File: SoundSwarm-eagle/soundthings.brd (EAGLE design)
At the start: 100 x 40 mm, 34 parts, among them Q1 IRLIB9343PbF, Q2 IRLB8721PBF, Q4 IRLB8721PBF

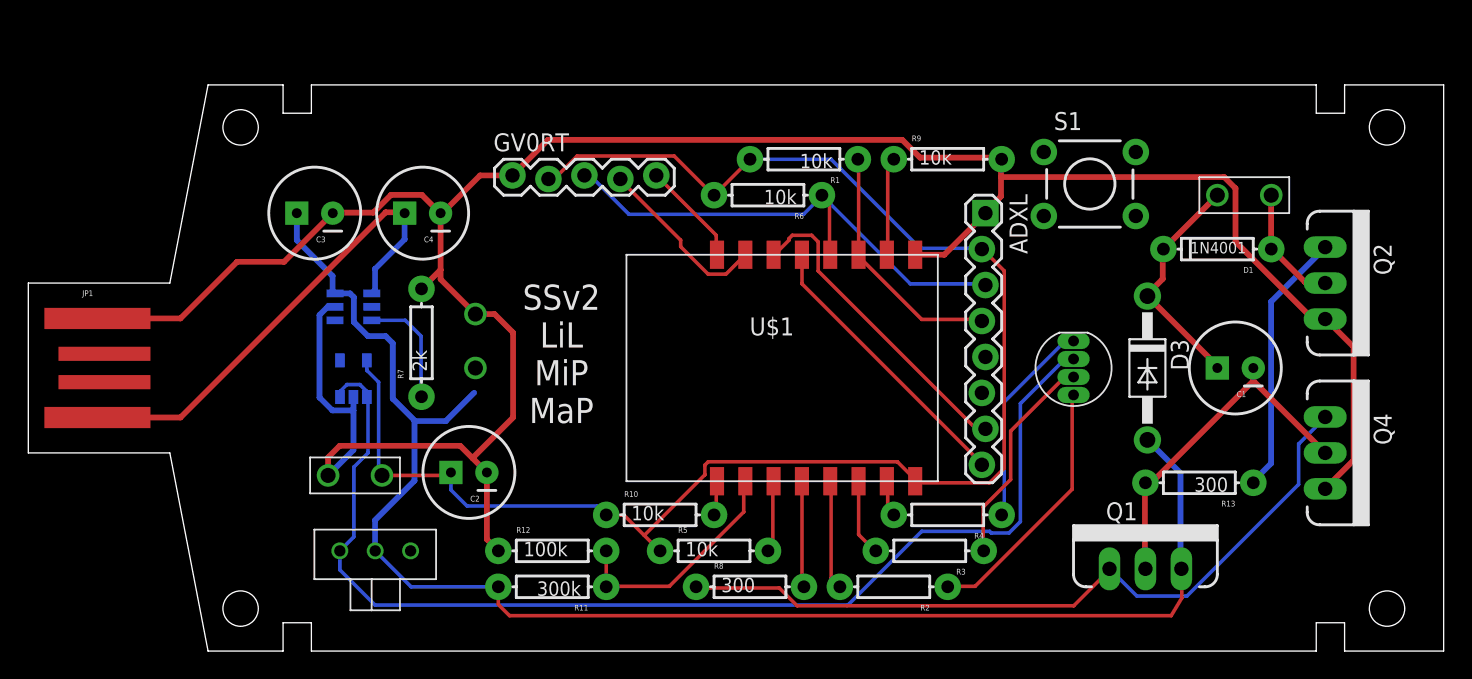
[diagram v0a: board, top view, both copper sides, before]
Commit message: removed names and added values
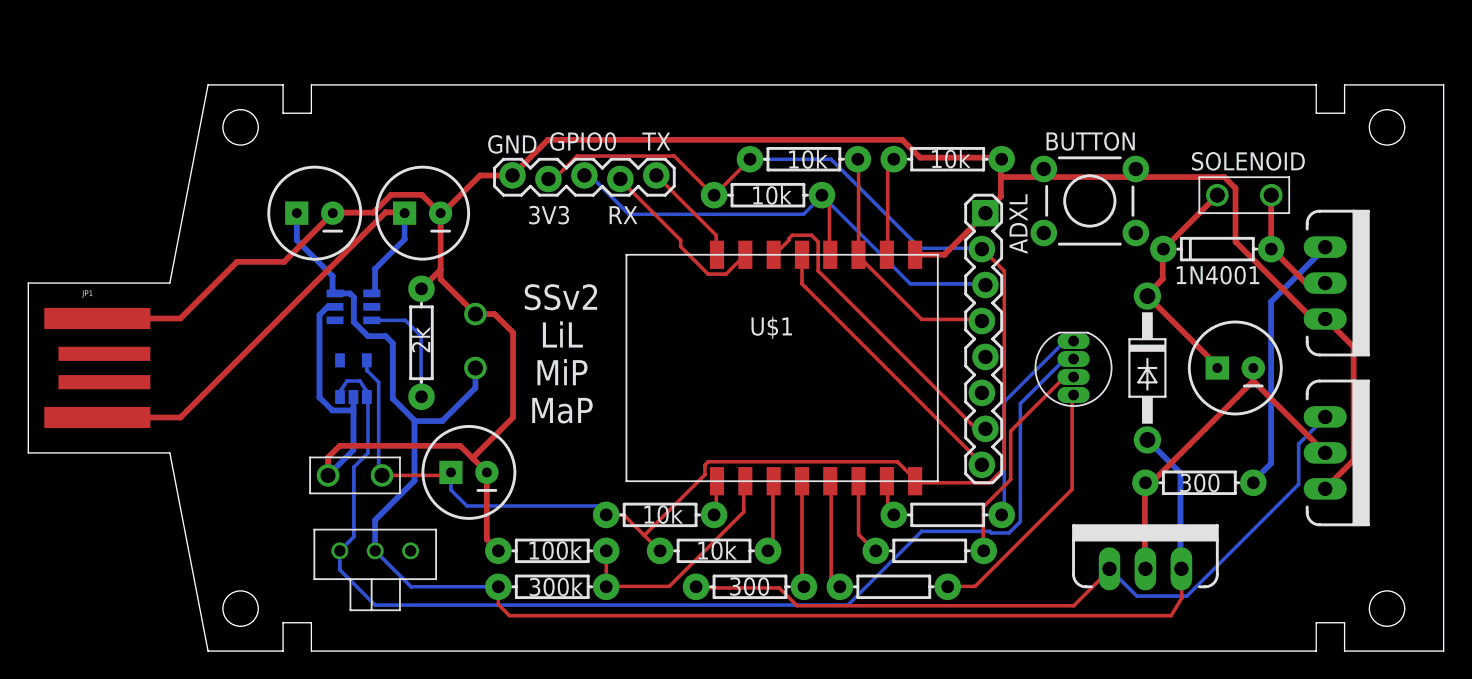
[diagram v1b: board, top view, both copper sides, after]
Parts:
- removed S1: SWITCH-MOMENTARY-2PTH, SparkFun-Electromechanical:TACTILE-PTH
- added BUTTON: SWITCH-MOMENTARY-2PTH, SparkFun-Electromechanical:TACTILE-PTH
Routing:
- net VBAT: track 107.8 -> 109.4 mm
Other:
- board text added: "3V3"
- board text added: "GND"
- board text added: "GPIO0"
- board text added: "RX"
- board text added: "SOLENOID"
- board text added: "TX"

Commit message: New schematic using DC-DC converter; needs Eagle-Lio-Library
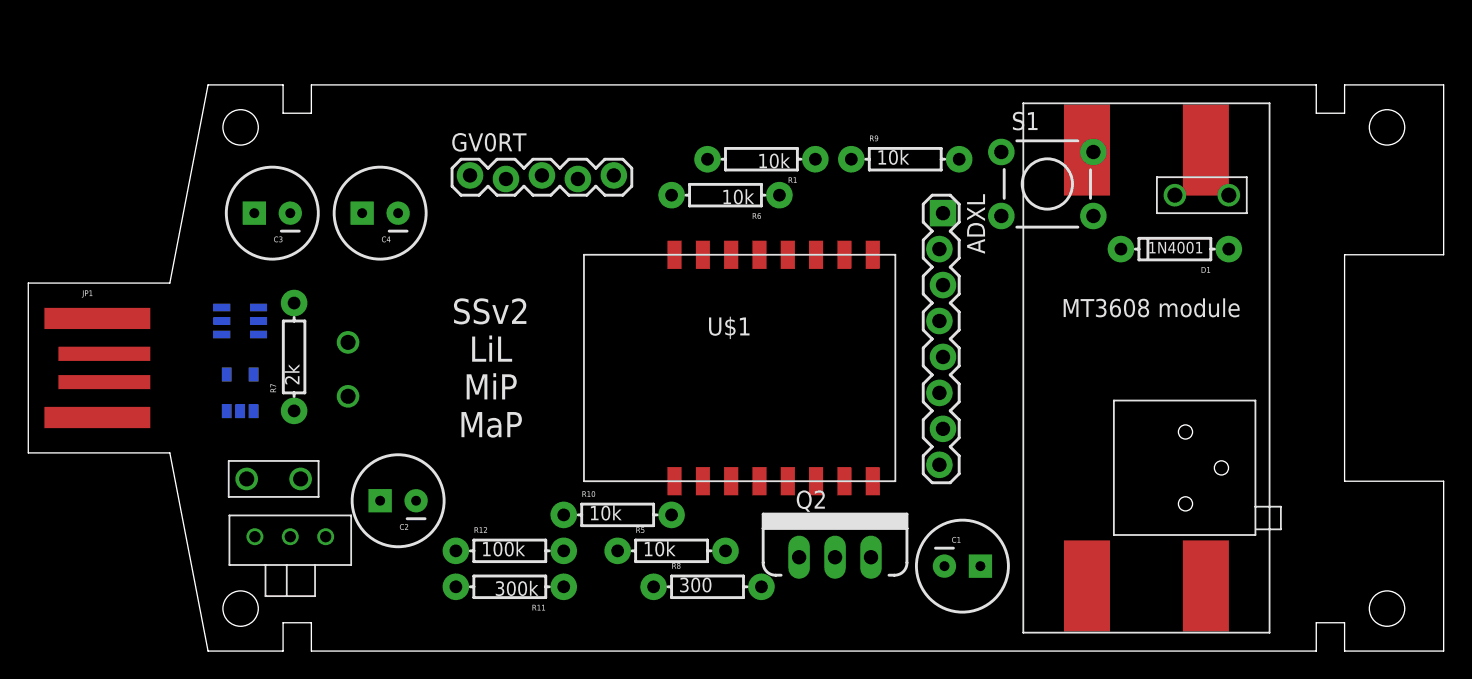
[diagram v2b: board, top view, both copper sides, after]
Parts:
- removed BUTTON: SWITCH-MOMENTARY-2PTH, SparkFun-Electromechanical:TACTILE-PTH
- removed D3: 1N5817, adafruit:DO41-10
- removed LED: LED-RGB-CA-THRUCLEAR, SparkFun-LED:LED-RGB-THRU
- removed Q1: IRLIB9343PbF, SparkFun-DiscreteSemi:TO220V
- removed Q4: IRLB8721PBF, SparkFun-DiscreteSemi:TO220V
- removed R13: 300, SparkFun-Passives:AXIAL-0.3
- removed R2, R3, R4: (no value), SparkFun-Passives:AXIAL-0.3
- added S1: SWITCH-MOMENTARY-2PTH, SparkFun-Electromechanical:TACTILE-PTH
- added U$7: MT3608, lio:MT3608
- C1: value 100uF -> 1000uF
- moved Q2 39.7 mm to (57.0, 6.63), turned to 0 degrees
- moved C1 23.8 mm to (66.0, 6.00), turned to 0 degrees
- moved BAT 9.22 mm to (22.6, 18.0)
- moved R7 9.06 mm to (18.8, 20.8)
- moved U$2 8.06 mm to (15.0, 23.3)
- moved U$5 8.06 mm to (15.0, 18.2)
- moved S2 6.08 mm to (18.5, 8.08)
- moved 3V3 5.76 mm to (19.2, 12.2)
- moved C2 5.39 mm to (26.1, 10.6)
- moved ADXL 3.00 mm to (64.5, 30.9)
- moved C3 3.00 mm to (17.2, 30.9)
- moved C4 3.00 mm to (24.9, 30.9)
- moved D1 3.00 mm to (81.0, 28.4)
- moved GV0RT 3.00 mm to (31.2, 33.5)
- moved R1 3.00 mm to (51.8, 34.8)
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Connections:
- removed net N$12: Q2.1, R13.P$1
- removed net N$14: LED.1, R4.P$1
- removed net N$2: LED.4, R2.P$1
- removed net N$4: C1.2, Q1.2, Q4.2, R13.P$2
- removed net N$9: LED.3, R3.P$1
- removed net VHI: C1.1, D1.C, D3.C, SOLENOID.P$1
- new net VOUT+: C1.1, D1.C, SOLENOID.P$1, U$7.VOUT+
- net GATE: now also Q2.1; no longer Q1.1, Q4.1
- net GND: now also C1.2, U$7.VIN-, U$7.VOUT-; no longer Q4.3
- net N$5: no longer R4.P$2
- net N$6: no longer R3.P$2
- net N$7: no longer R2.P$2
- net VBAT: now also U$7.VIN+; no longer D3.A, Q1.3
- net VDD: no longer LED.2
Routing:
- net GND: track 183.0 -> 0.00 mm
- net 3.3V: track 113.1 -> 0.00 mm
- net VBAT: track 109.4 -> 0.00 mm
- net VDD: track 81.7 -> 0.00 mm
- net GATE: track 53.9 -> 0.00 mm
- net CS: track 37.2 -> 0.00 mm
- net 5V: track 34.4 -> 0.00 mm
- net N$4: track 24.8 -> 0.00 mm
- net SDA: track 22.5 -> 0.00 mm
- net SCL: track 20.1 -> 0.00 mm
- net N$12: track 18.7 -> 0.00 mm
- net N$2: track 18.4 -> 0.00 mm
- net INT: track 17.6 -> 0.00 mm
- net ADC: track 16.7 -> 0.00 mm
- net VHI: track 16.3 -> 0.00 mm
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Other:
- outline, holes or cut-outs redrawn
- board text removed: "3V3"
- board text removed: "GND"
- board text removed: "GPIO0"
- board text removed: "RX"
- board text removed: "SOLENOID"
- board text removed: "TX"

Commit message: Fixed PCB layout v2
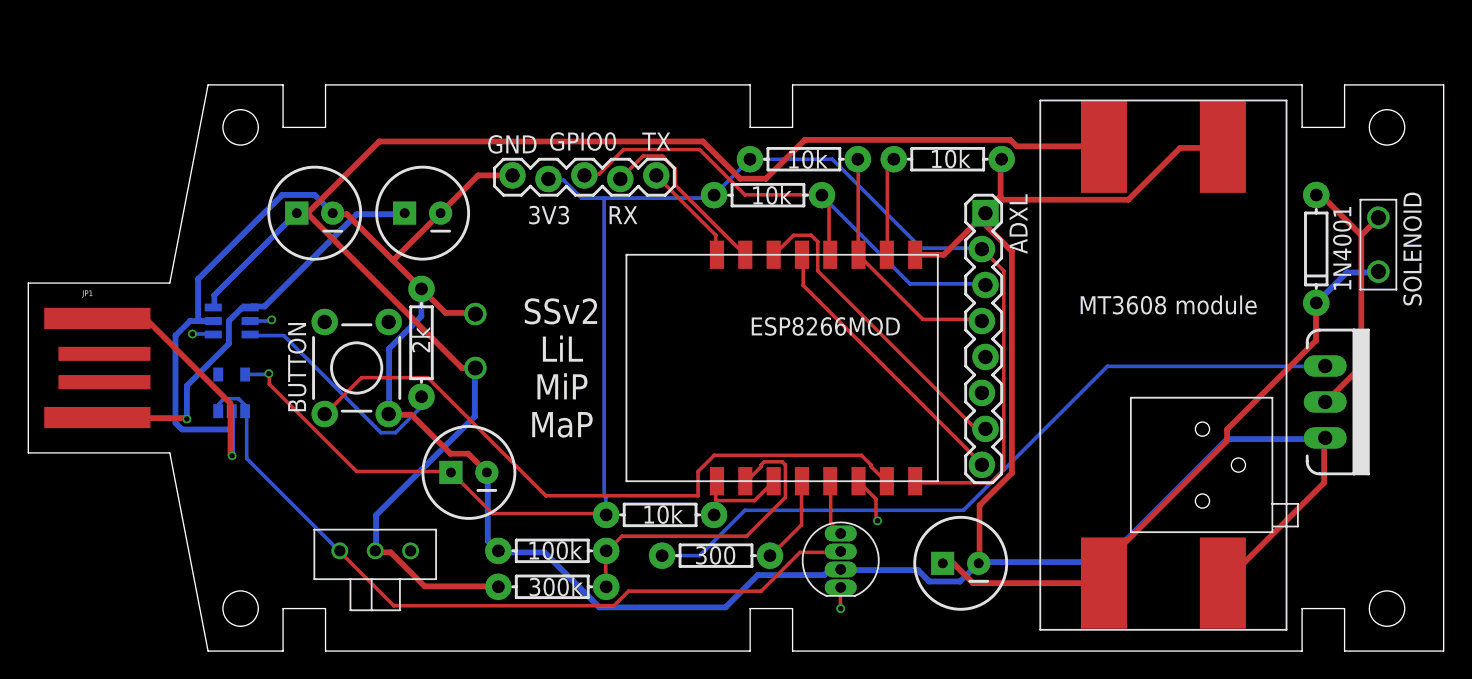
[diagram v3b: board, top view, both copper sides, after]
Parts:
- removed R5: 10k, SparkFun-Passives:AXIAL-0.3
- removed S1: SWITCH-MOMENTARY-2PTH, SparkFun-Electromechanical:TACTILE-PTH
- removed U$1: ESP8266-07, lio:ESP-07
- added !CHRG, !STDBY, 5V, DOUT, GND, GPIO12: TEST-POINTTP_15TH_THRU, SparkFun-Passives:TP_15TH
- added BUTTON: SWITCH-MOMENTARY-2PTH, SparkFun-Electromechanical:TACTILE-PTH
- added ESP8266MOD: ESP8266-07, lio:ESP-07
- added L1: WS2812BTH, lio:WS2812F5
- 3V3: value (none) -> TEST-POINTTP_15TH_THRU; device SparkFun-Connectors:1X02_BIG -> SparkFun-Passives:TP_15TH
- C1: value 1000uF -> 100uF
- moved Q2 36.3 mm to (91.6, 17.6), turned to 270 degrees
- moved SOLENOID 15.4 mm to (95.4, 26.8), turned to 90 degrees
- moved D1 9.99 mm to (91.0, 28.4), turned to 270 degrees
- moved BAT 9.22 mm to (31.6, 20.0)
- moved R7 9.06 mm to (27.8, 21.8)
- moved 3V3 7.77 mm to (17.0, 19.6), turned to 0 degrees
- moved S2 6.08 mm to (24.5, 7.08)
- moved C2 5.39 mm to (31.1, 12.6)
- moved ADXL 3.00 mm to (67.5, 30.9)
- moved C3 3.00 mm to (20.2, 30.9)
- moved C4 3.00 mm to (27.9, 30.9)
- moved GV0RT 3.00 mm to (34.2, 33.5)
- moved R1 3.00 mm to (54.8, 34.8)
- moved R10 3.00 mm to (44.6, 9.62)
- moved R11 3.00 mm to (37.0, 4.54)
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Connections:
- net N$1 renamed SOL-
- removed net N$15: GV0RT.5, U$1.TXD
- removed net N$16: GV0RT.4, U$1.RXD
- removed net N$19: R9.P$1, U$1.GPIO15
- removed net N$20: R10.P$2, U$1.REST
- removed net N$5: U$1.GPIO13
- removed net N$7: U$1.GPIO14
- new net DIN: ESP8266MOD.GPIO14, L1.4
- new net DOUT: DOUT.P$1, L1.1
- new net EN: ESP8266MOD.CH_PD, ESP8266MOD.REST, R10.P$2
- new net GPIO13: BUTTON.1, ESP8266MOD.GPIO13
- new net GPIO15: ESP8266MOD.GPIO15, R9.P$1
- new net N$8: !CHRG.P$1, U$2.1
- new net RX: ESP8266MOD.RXD, GV0RT.4
- new net TX: ESP8266MOD.TXD, GV0RT.5
- net 3.3V: now also ESP8266MOD.VCC; no longer R5.P$1, U$1.VCC
- net 5V: now also 5V.P$1
- net ADC: now also ESP8266MOD.ADC; no longer U$1.ADC
- net CS: now also ESP8266MOD.GPIO0; no longer U$1.GPIO0
- net GND: now also BUTTON.3, ESP8266MOD.GND, GND.P$1, L1.2; no longer 3V3.P$2, U$1.GND
- net GPIO16: now also ESP8266MOD.GPIO16; no longer U$1.GPIO16
- net INT: now also ESP8266MOD.GPIO2; no longer U$1.GPIO2
- net N$3: now also !STDBY.P$1, U$2.5; no longer R5.P$2, U$1.CH_PD
- net N$6: now also ESP8266MOD.GPIO12, GPIO12.P$1; no longer U$1.GPIO12
- net SCL: now also ESP8266MOD.GPIO5; no longer U$1.GPIO5
- net SDA: now also ESP8266MOD.GPIO4; no longer U$1.GPIO4
- net VDD: now also L1.3
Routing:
- net GND: track 0.00 -> 229.7 mm
- net VBAT: track 0.00 -> 113.5 mm
- net 3.3V: track 0.00 -> 110.5 mm
- net VDD: track 0.00 -> 54.5 mm
- net GATE: track 0.00 -> 52.4 mm
- net GPIO13: track 0.00 -> 47.2 mm
- net VOUT+: track 0.00 -> 43.3 mm
- net CS: track 0.00 -> 37.6 mm
- net 5V: track 0.00 -> 30.1 mm
- net ADC: track 0.00 -> 22.6 mm
- net SDA: track 0.00 -> 22.4 mm
- net SCL: track 0.00 -> 20.1 mm
- net SOL-: track 0.00 -> 19.0 mm
- net INT: track 0.00 -> 17.5 mm
- net N$11: track 0.00 -> 16.4 mm
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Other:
- outline, holes or cut-outs redrawn
- board text added: "3V3"
- board text added: "GND"
- board text added: "GPIO0"
- board text added: "RX"
- board text added: "SOLENOID"
- board text added: "TX"

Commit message: ERC and DRC passed; rotated wifi
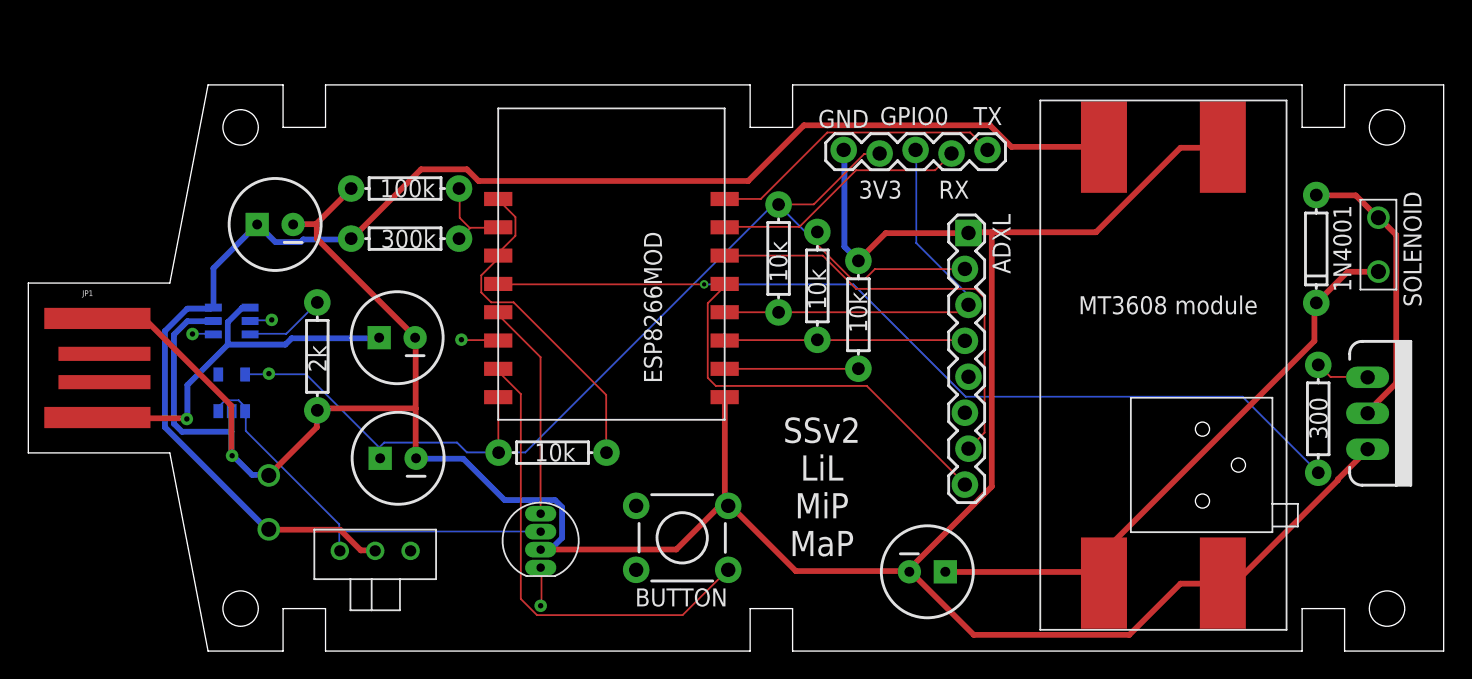
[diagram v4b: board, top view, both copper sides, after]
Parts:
- moved R8 43.6 mm to (91.1, 16.4), turned to 270 degrees
- moved GPIO12 32.1 mm to (30.6, 22.0)
- moved R12 27.6 mm to (26.6, 32.7)
- moved R11 26.7 mm to (26.6, 29.1)
- moved BUTTON 25.9 mm to (46.2, 8.00), turned to 180 degrees
- moved GV0RT 23.5 mm to (57.6, 35.3)
- moved L1 21.2 mm to (36.2, 7.80)
- moved DOUT 21.2 mm to (36.2, 3.20)
- moved BAT 18.5 mm to (17.0, 8.60)
- moved ESP8266MOD 13.9 mm to (41.2, 28.3), turned to 270 degrees
- moved R9 12.7 mm to (58.6, 23.8), turned to 90 degrees
- moved R1 9.00 mm to (55.8, 25.8), turned to 90 degrees
- moved C4 8.98 mm to (26.1, 22.1)
- moved R10 8.78 mm to (37.0, 14.0)
- moved R7 7.42 mm to (20.4, 20.8), turned to 270 degrees
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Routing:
- net GPIO16: track 6.22 -> 63.5 mm, vias 0 -> 1
- net GATE: track 52.4 -> 3.86 mm
- net 3.3V: track 110.5 -> 77.8 mm
- net VDD: track 54.5 -> 29.8 mm
- net EN: track 7.12 -> 24.1 mm
- net ADC: track 22.6 -> 6.22 mm
- net GPIO13: track 47.2 -> 33.4 mm
- net TX: track 7.46 -> 21.0 mm
- net VBAT: track 113.5 -> 101.6 mm
- net DIN: track 3.99 -> 15.5 mm
- net N$11: track 16.4 -> 5.71 mm
- net SCL: track 20.1 -> 28.5 mm
- net SDA: track 22.4 -> 30.7 mm
- net CS: track 37.6 -> 29.9 mm
- net RX: track 13.1 -> 18.2 mm
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
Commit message: Move away from the edges; add labels
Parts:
- moved DOUT 3.61 mm to (39.2, 5.20)
- moved !STDBY 1.28 mm to (18.0, 24.4)
- moved 5V 1.22 mm to (12.4, 16.6)
- moved 3V3 1.00 mm to (18.0, 19.6)
- moved U$5 1.00 mm to (15.4, 18.2)
- moved U$2 0.60 mm to (15.0, 23.3)
- moved R7 0.60 mm to (21.0, 20.8)
- moved !CHRG 0.20 mm to (11.8, 22.4)
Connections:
- net N$3 renamed !STDBY
- net N$6 renamed GPIO12
- net N$8 renamed !CHRG
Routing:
- net GND: track 229.6 -> 233.1 mm
- net !STDBY: track 1.57 -> 3.39 mm
- net EN: track 24.1 -> 25.7 mm
- net VBAT: track 101.6 -> 102.7 mm
- net N$11: track 5.71 -> 6.82 mm
- net 3.3V: track 77.8 -> 78.9 mm
- net !CHRG: track 1.49 -> 2.23 mm
- net SOL-: track 20.2 -> 20.8 mm
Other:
- board text added: "!CHRG"
- board text added: "!STDBY"
- board text added: "+"
- board text added: "12"
- board text added: "5V"
- board text added: "BAT"
- board text added: "CS"
- board text added: "INT"
- board text added: "LED"
- board text added: "OFF"
- board text added: "ON"
- board text added: "Only a prophet of the infinite may ignite this rekindling of growth."
- board text added: "SCA"
- board text added: "SCL"
- board text added: "VIN+"
- board text added: "VOUT+"

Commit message: As submitted to ditrypcbs
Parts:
- removed GPIO12: TEST-POINTTP_15TH_THRU, SparkFun-Passives:TP_15TH
- added D6: TEST-POINTTP_15TH_THRU, SparkFun-Passives:TP_15TH
- moved R8 43.9 mm to (47.2, 15.3), turned to 180 degrees
- moved Q2 3.58 mm to (91.4, 18.4)
- moved SOLENOID 2.86 mm to (94.2, 29.4)
- moved D1 2.51 mm to (89.8, 30.6)
- moved U$7 2.09 mm to (79.6, 22.2)
- moved L1 2.00 mm to (36.2, 9.80)
- moved !CHRG 2.00 mm to (11.8, 24.4)
- moved !STDBY 2.00 mm to (18.0, 26.4)
- moved 3V3 2.00 mm to (18.0, 21.6)
- moved 5V 2.00 mm to (12.4, 18.6)
- moved ADXL 2.00 mm to (66.3, 31.5)
- moved BAT 2.00 mm to (17.0, 10.6)
- moved BUTTON 2.00 mm to (46.2, 10.0)
- moved C1 2.00 mm to (63.5, 7.60)
- moved C2 2.00 mm to (26.1, 15.6)
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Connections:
- net DIN renamed GPIO14
- net GPIO12: now also D6.P$1; no longer GPIO12.P$1
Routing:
- net GPIO16: track 63.5 -> 16.9 mm, vias 1 -> 0
- net GATE: track 3.86 -> 42.8 mm
- net GND: track 233.1 -> 221.2 mm
- net GPIO13: track 33.8 -> 30.4 mm
- net EN: track 25.7 -> 24.4 mm
- net !STDBY: track 3.39 -> 2.21 mm
- net N$11: track 6.82 -> 5.68 mm
- net VBAT: track 102.7 -> 102.0 mm
- net 3.3V: track 78.9 -> 78.2 mm
- net VOUT+: track 43.4 -> 42.9 mm
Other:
- board size 100 x 40 mm -> 100 x 44 mm
- board text added: "D3"
- board text added: "D6"
- board text removed: "12"
- board text removed: "GPIO0"
